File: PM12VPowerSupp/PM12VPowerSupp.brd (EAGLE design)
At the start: 82.2 x 86.3 mm, 29 parts

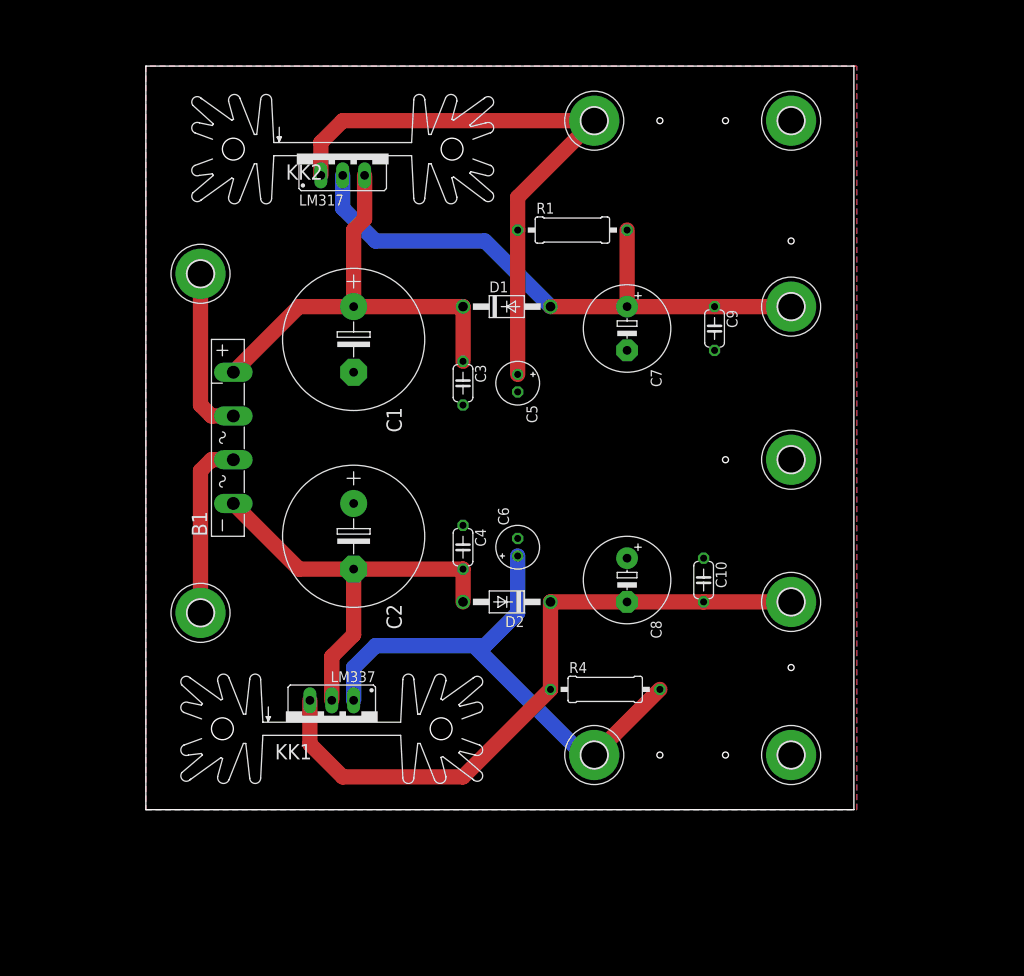
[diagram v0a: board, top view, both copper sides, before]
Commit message: Revert "No more air wires. Have to do relief holes and heat sinks"
This reverts commit 0472ab177aecc554d98bdcb29c09631f317f4fda.
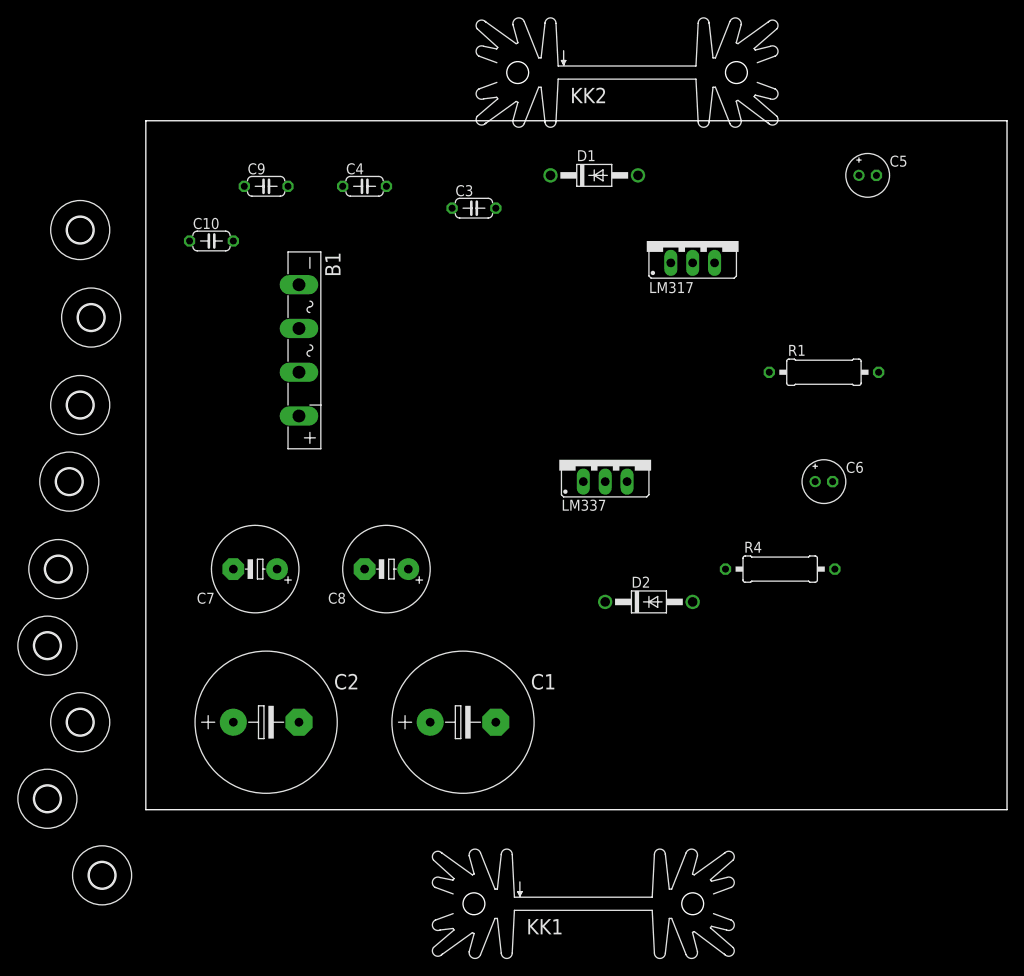
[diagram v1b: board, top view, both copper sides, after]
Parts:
- removed AC1, AC2, POS_TRIM_LEAD: MOUNT-PAD-ROUND3.0, holes:3,0-PAD
- added AC1_INPUT, AC2_INPPUT, H1: MOUNT-HOLE3.0, holes:3,0
- GND, NEG_TRIM_GND, NEG_TRIM_LEAD, POS_TRIM_GND, VDC+, VDC-: value MOUNT-PAD-ROUND3.0 -> MOUNT-HOLE3.0; device holes:3,0-PAD -> holes:3,0
- moved GND 99.8 mm to (-10.2, 27.9)
- moved NEG_TRIM_GND 87.3 mm to (-11.4, 19.1)
- moved VDC- 85.0 mm to (-8.89, 38.1), turned to 0 degrees
- moved VDC+ 83.0 mm to (-7.62, 67.3)
- moved POS_TRIM_GND 82.9 mm to (-6.35, 57.1)
- moved C10 69.4 mm to (7.62, 66.0), turned to 0 degrees
- moved NEG_TRIM_LEAD 58.8 mm to (-5.08, -7.62)
- moved C9 54.6 mm to (14.0, 72.4), turned to 0 degrees
- moved C7 51.4 mm to (12.7, 27.9), turned to 180 degrees
- moved C5 47.3 mm to (83.8, 73.7), turned to 0 degrees
- moved C1 46.2 mm to (36.8, 10.2), turned to 0 degrees
- moved LM337 44.0 mm to (53.3, 40.6), turned to 0 degrees
- moved C4 43.4 mm to (25.4, 72.4), turned to 0 degrees
- moved LM317 41.9 mm to (63.5, 66.0)
- moved C6 36.4 mm to (78.7, 38.1), turned to 0 degrees
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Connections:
- removed net AC1_INPUT: AC1.B3,0, B1.AC1
- removed net NEG_TRIM: C6.+, LM337.1, NEG_TRIM_LEAD.B3,0, R4.2
- removed net POS_TRIM: C5.+, LM317.1, POS_TRIM_LEAD.B3,0, R1.1
- new net N$2: C6.+, LM337.1, R4.2
- new net N$3: B1.AC2
- new net POS_TRIM_LEAD: C5.+, LM317.1, R1.1
- net GND: no longer GND.B3,0, NEG_TRIM_GND.B3,0, POS_TRIM_GND.B3,0
- net N$1: now also B1.AC1; no longer AC2.B3,0, B1.AC2
- net VDC+: no longer VDC+.B3,0
- net VDC-: no longer VDC-.B3,0
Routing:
- net VDC-: track 76.9 -> 0.00 mm
- net POS_TRIM: track 69.8 -> 0.00 mm
- net VDC+: track 69.5 -> 0.00 mm
- net NEG_TRIM: track 62.1 -> 0.00 mm
- net N$5: track 51.9 -> 0.00 mm
- net N$4: track 49.9 -> 0.00 mm
- net N$1: track 20.8 -> 0.00 mm
- net AC1_INPUT: track 19.6 -> 0.00 mm
- removed copper zone on layer 1, net GND
- removed copper zone on layer 16, net GND
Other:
- board size 82.2 x 86.3 mm -> 100 x 80 mm

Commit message: No more air wires. Have to do relief holes and heat sinks
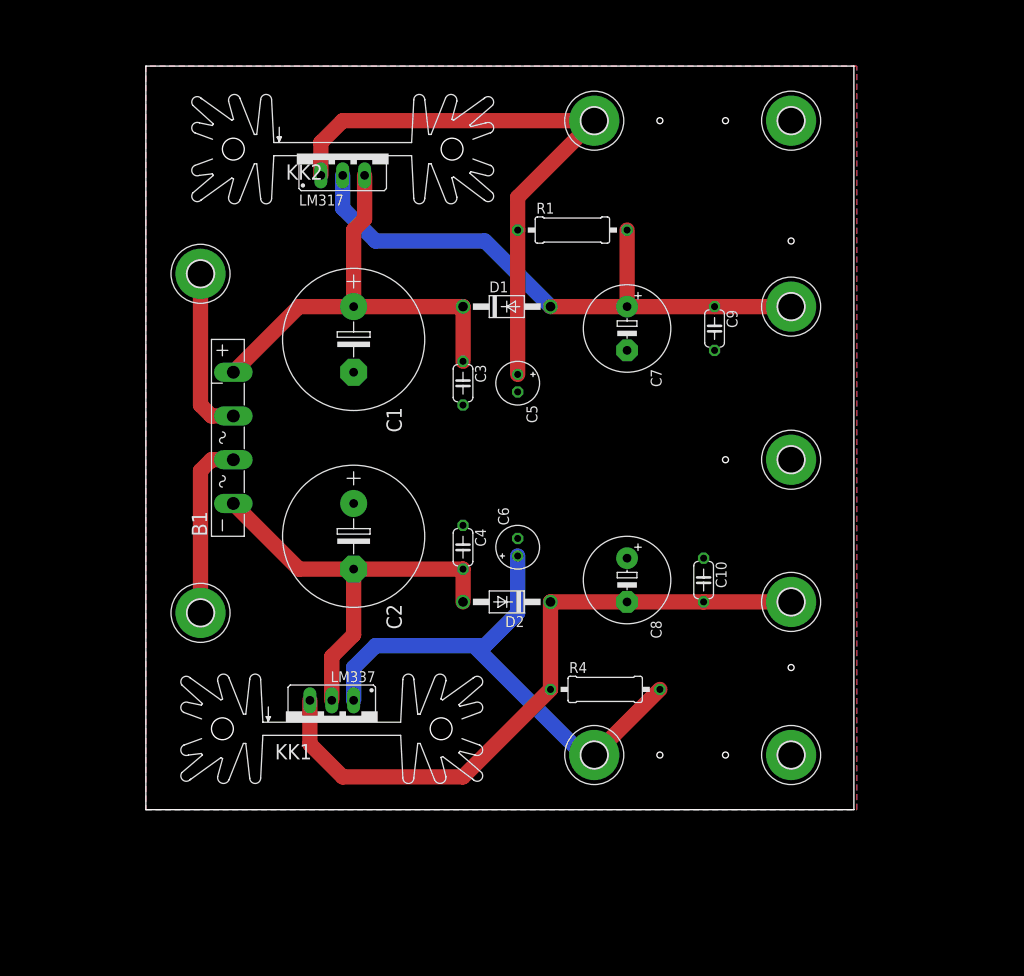
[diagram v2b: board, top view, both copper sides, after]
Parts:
- removed AC1_INPUT, AC2_INPPUT, H1: MOUNT-HOLE3.0, holes:3,0
- added AC1, AC2, POS_TRIM_LEAD: MOUNT-PAD-ROUND3.0, holes:3,0-PAD
- GND, NEG_TRIM_GND, NEG_TRIM_LEAD, POS_TRIM_GND, VDC+, VDC-: value MOUNT-HOLE3.0 -> MOUNT-PAD-ROUND3.0; device holes:3,0 -> holes:3,0-PAD
- moved GND 99.8 mm to (74.9, 80.0)
- moved NEG_TRIM_GND 87.3 mm to (74.9, 6.35)
- moved VDC- 85.0 mm to (74.9, 24.1), turned to 90 degrees
- moved VDC+ 83.0 mm to (74.9, 58.4)
- moved POS_TRIM_GND 82.9 mm to (74.9, 40.6)
- moved C10 69.4 mm to (64.8, 26.7), turned to 270 degrees
- moved NEG_TRIM_LEAD 58.8 mm to (52.1, 6.35)
- moved C9 54.6 mm to (66.0, 55.9), turned to 270 degrees
- moved C7 51.4 mm to (55.9, 55.9), turned to 270 degrees
- moved C5 47.3 mm to (43.2, 49.5), turned to 270 degrees
- moved C1 46.2 mm to (24.1, 54.6), turned to 270 degrees
- moved LM337 44.0 mm to (21.6, 10.2), turned to 180 degrees
- moved C4 43.4 mm to (36.8, 30.5), turned to 270 degrees
- moved LM317 41.9 mm to (22.9, 76.2)
- moved C6 36.4 mm to (43.2, 30.5), turned to 90 degrees
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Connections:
- removed net N$2: C6.+, LM337.1, R4.2
- removed net N$3: B1.AC2
- removed net POS_TRIM_LEAD: C5.+, LM317.1, R1.1
- new net AC1_INPUT: AC1.B3,0, B1.AC1
- new net NEG_TRIM: C6.+, LM337.1, NEG_TRIM_LEAD.B3,0, R4.2
- new net POS_TRIM: C5.+, LM317.1, POS_TRIM_LEAD.B3,0, R1.1
- net GND: now also GND.B3,0, NEG_TRIM_GND.B3,0, POS_TRIM_GND.B3,0
- net N$1: now also AC2.B3,0, B1.AC2; no longer B1.AC1
- net VDC+: now also VDC+.B3,0
- net VDC-: now also VDC-.B3,0
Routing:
- net VDC-: track 0.00 -> 76.9 mm
- net POS_TRIM: track 0.00 -> 69.8 mm
- net VDC+: track 0.00 -> 69.5 mm
- net NEG_TRIM: track 0.00 -> 62.1 mm
- net N$5: track 0.00 -> 51.9 mm
- net N$4: track 0.00 -> 49.9 mm
- net N$1: track 0.00 -> 20.8 mm
- net AC1_INPUT: track 0.00 -> 19.6 mm
- added copper zone on layer 1, net GND
- added copper zone on layer 16, net GND
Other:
- board size 100 x 80 mm -> 82.2 x 86.3 mm
